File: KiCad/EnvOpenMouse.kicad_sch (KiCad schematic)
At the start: 55 parts, among them J11 Conn_02x02_Top_Bottom, J2 Button, J4 Conn_02x02_Top_Bottom, J5 Conn_02x02_Top_Bottom, J5 SKRKAEE020, J6 Conn_02x02_Top_Bottom, J7 Conn_02x02_Top_Bottom, J8 Conn_02x02_Top_Bottom, J9 Conn_01x03, SW1 SW_Push_SPDT, SW2 SW_Push_SPDT, SW3 SW_Push_SPDT, U1 AP2112K-3.3, U2 TLV70218DBVR, U3 RP2040, U4 PMW3360DM-T2QU, Y1 3225_4P 12MHz

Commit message: redid all traces, adjusted schematic, pinouts, added some side buttons.
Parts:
- removed C10, C11, C12, C13, C14, C5, C6, C7, C8, C9: 100nf 0402, Capacitor_SMD:C_0402_1005Metric, symbol Device:C
- removed C15, C16, C3: 1uf 0402, Capacitor_SMD:C_0402_1005Metric, symbol Device:C
- removed C19, C2: 22pf 0402, Capacitor_SMD:C_0402_1005Metric, symbol Device:C
- removed C2: 0.1uf 0402, Capacitor_SMD:C_0402_1005Metric, symbol Device:C
- removed C3: 10uf 0402 6.3V, Capacitor_SMD:C_0402_1005Metric, symbol Device:C
- removed C5: 10uf 0402, Capacitor_SMD:C_0402_1005Metric, symbol Device:C
- removed D1: 1n4002W, Diode_SMD:D_SOD-123, symbol Device:D_Schottky
- removed FLASH1: W25Q16JVUXIQ, Package_SON:SON-8-1EP_3x2mm_P0.5mm_EP1.4x1.6mm, symbol Memory_Flash:W25Q32JVZP
- removed J2: Button, Button_Switch_SMD:SW_Push_SPST_NO_Alps_SKRK, symbol Switch:SW_Push
- removed J5: SKRKAEE020, Button_Switch_SMD:SW_Push_SPST_NO_Alps_SKRK, symbol Switch:SW_Push
- removed R1, R3: 5.1K, Resistor_SMD:R_0402_1005Metric, symbol Device:R_Small
- removed R1, R11: 1K 0402, Resistor_SMD:R_0402_1005Metric, symbol Device:R
- removed R10, R9: 27Ohms 0402 Resistor, Capacitor_SMD:C_0402_1005Metric, symbol Device:R
- removed R2: 10K 0402, Resistor_SMD:R_0402_1005Metric, symbol Device:R
- removed R4: 10k 0402, Resistor_SMD:R_0402_1005Metric, symbol Device:R
- removed U1: AP2112K-3.3, Package_TO_SOT_SMD:SOT-23-5, symbol Regulator_Linear:AP2112K-3.3
- removed U2: TLV70218DBVR, Package_TO_SOT_SMD:SOT-23-5, symbol Regulator_Linear:TLV70218_SOT23-5
- removed U3: RP2040, RP2040_minimal:RP2040-QFN-56, symbol MCU_RaspberryPi_RP2040:RP2040
- removed Y1: 3225_4P 12MHz, Crystal:Crystal_SMD_3225-4Pin_3.2x2.5mm, symbol Device:Crystal_GND24
- removed e1: TYPE-C-31-M-12, HRO-TYPE-C31-M-12:HRO-TYPE-C-31-M-12, symbol Type-C:HRO-TYPE-C-31-M-12
- added H5, H6, H7, H8: MountingHole_Pad, MountingHole:MountingHole_2.2mm_M2, symbol Mechanical:MountingHole_Pad
- added J10, J12, J13: 0.8mm BM03B, Connector_JST:JST_SUR_BM03B-SURS-TF_1x03-1MP_P0.80mm_Vertical, symbol Connector_Generic:Conn_01x03
- added SW4, SW5, SW6, SW7: SW_Push_SPDT, Button_Switch_SMD:SW_SPST_B3U-1000P, symbol Switch:SW_Push
- J9: value Conn_01x03 -> 0.8mm BM03B; footprint Connector_PinHeader_1.27mm:PinHeader_1x03_P1.27mm_Vertical -> Connector_JST:JST_SUR_BM03B-SURS-TF_1x03-1MP_P0.80mm_Vertical
- SW1, SW2, SW3: symbol Switch:SW_Push_SPDT -> Switch:SW_Push
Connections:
- net MB-1-B_MB is gone; now on net GND: J8.1 (Pin_1)
- net MB-2-B_MB is gone; now on net GND: J7.4 (Pin_4)
- net MB-3-B_MB is gone; now on net GND: J8.4 (Pin_4)
- net GND: now also J5.4 (Pin_4), J6.1 (Pin_1), J6.4 (Pin_4), SW1.1, SW2.1, SW3.1, H5.1, H6.1, H7.1, H8.1, J10.2 (Pin_2), J12.2 (Pin_2), J13.2 (Pin_2), SW4.1, SW5.1, SW6.1, SW7.1
- net MB-1-A: now also SW1.2; no longer SW1.1 (A)
- net MB-2-A: now also SW2.2; no longer SW2.1 (A)
- net MB-3-A: now also SW3.2; no longer SW3.1 (A)
- removed net MB-1-B: J6.1 (Pin_1), SW1.2 (B)
- removed net MB-2-B: J5.4 (Pin_4), SW2.2 (B)
- removed net MB-3-B: J6.4 (Pin_4), SW3.2 (B)
- net SWCLK renamed SB-2-A
- net SB-2-A: now also SW5.2
- net SWD renamed SB-1-A
- net SB-1-A: now also SW4.2
- new net SB-1-A_MB: J12.1 (Pin_1)
- new net SB-2-A_MB: J12.3 (Pin_3)
- new net SB-3-A: J10.1 (Pin_1), SW6.2
- new net SB-3-A_MB: J13.1 (Pin_1)
- new net SB-4-A: J10.3 (Pin_3), SW7.2
- new net SB-4-A_MB: J13.3 (Pin_3)
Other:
- added sheet Power and USB (Power_USB.kicad_sch)
- added sheet RP2040 (RP2040.kicad_sch)
- note added: "IC to use - DRV2605L"
- note added: "LRM motor - C2682305"
- note added: "Main mouse buttons"
- note removed: "1.8V regulator"
- note removed: "1K resistor to prevent overdriving of the crystal as per the minimal design example"
- note removed: "2x 5.1K Resistors on the CC pins will = 5V@1.5A this is the recomended default config for type-c"
- note removed: "3.3V regulator"
- note removed: "Crystal"
- note removed: "D1 NEEDS to be 0omh resistor or 1n4002"
- note removed: "Flash"
- note removed: "KoreanHROParts USB_C_Receptacle_HRO_TYPE-C-31-M-12"
- note removed: "Make sure C10 is close to pin 44 of RP2040"
- note removed: "Make sure C3 is close to pin 45 of RP2040"
- note removed: "Make sure R3 and R4 are close to RP2040"
- note removed: "Make sure the flash chip you have selected supports 3.3V power or adjust the design."
- note removed: "Mouse Buttons"
- note removed: "Pin 9 technically doesnt exist its the main central contact under the chip for heat dicipation"
- note removed: "RP2040 supports 1MHz to 15MHz"
- note removed: "These decoupling capacitors are meant to be put close by each 3.3V pin of the RP2040"
- note removed: "USB/POWER"
- note removed: "not 22pf but pick to match crystal."
- note removed: "this is for factory testing always pull this to ground"
- moved on the sheet: C8, C9, H1, H2, H3, H4, J11, J4, J5, J6, J7, J8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

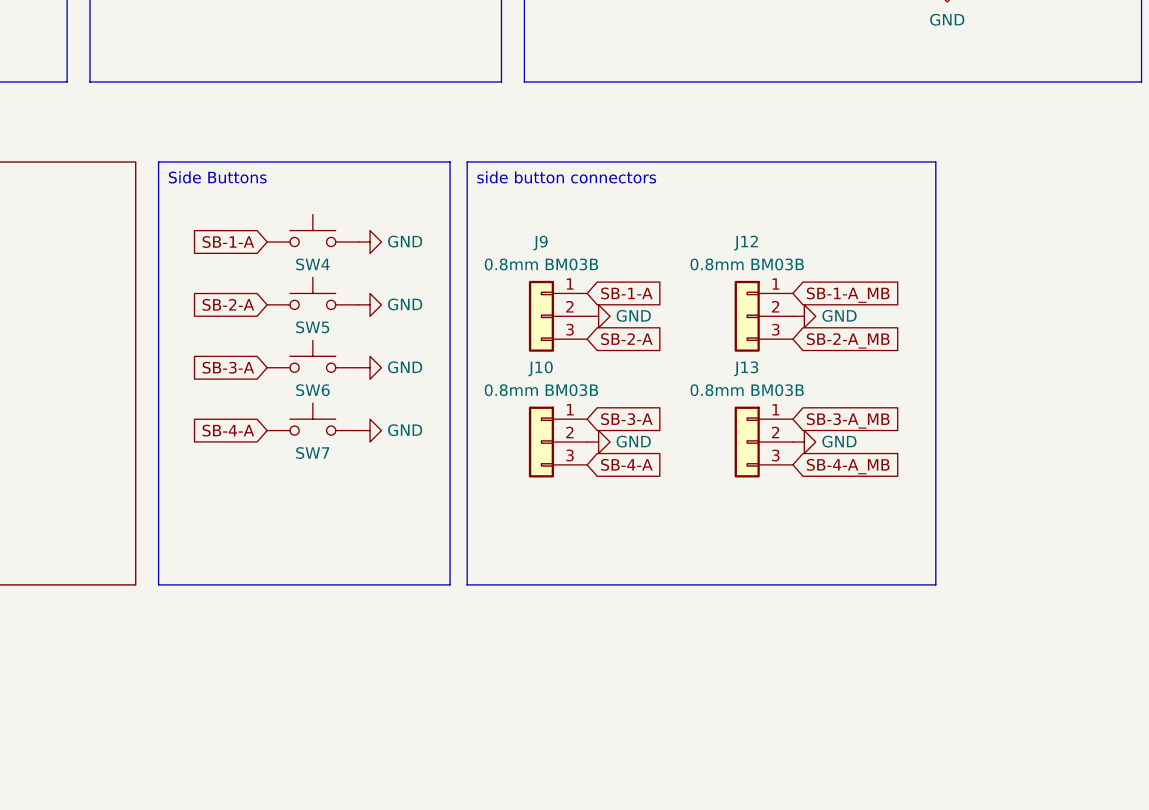
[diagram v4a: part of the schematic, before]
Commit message: downsized main board, added more buttons and respective connector, improved spacing of various power traces
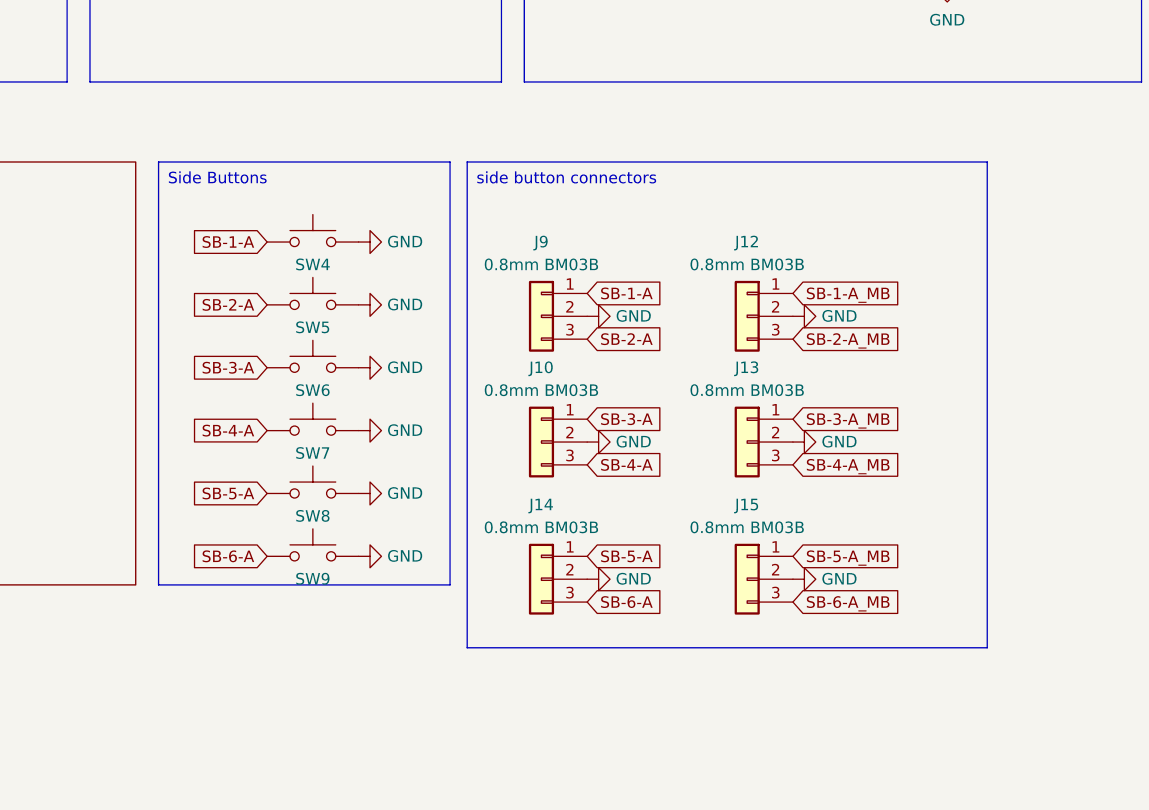
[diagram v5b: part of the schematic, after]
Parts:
- added J14, J15: 0.8mm BM03B, Connector_JST:JST_SUR_BM03B-SURS-TF_1x03-1MP_P0.80mm_Vertical, symbol Connector_Generic:Conn_01x03
- added SW8, SW9: SW_Push_SPDT, Button_Switch_SMD:SW_SPST_B3U-1000P, symbol Switch:SW_Push
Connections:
- net GND: now also J14.2 (Pin_2), J15.2 (Pin_2), SW8.1, SW9.1
- new net SB-5-A: J14.1 (Pin_1), SW8.2
- new net SB-5-A_MB: J15.1 (Pin_1)
- new net SB-6-A: J14.3 (Pin_3), SW9.2
- new net SB-6-A_MB: J15.3 (Pin_3)

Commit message: generated production files
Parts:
- J4: footprint Connector_PinHeader_1.27mm:PinHeader_1x02_P1.27mm_Vertical -> Connector_PinSocket_1.27mm:PinSocket_1x02_P1.27mm_Vertical
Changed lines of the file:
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@@
 			)
 		)
-		(property "Footprint" "Connector_PinHeader_1.27mm:PinHeader_1x02_P1.27mm_Vertical"
+		(property "Footprint" "Connector_PinSocket_1.27mm:PinSocket_1x02_P1.27mm_Vertical"
 			(at 36.83 30.48 0)
 			(effects

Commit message: final cleanups and other fixes
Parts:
- H1, H2, H3, H4, H5, H6, H7, H8: now left out of the parts list
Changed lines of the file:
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@@
 		(unit 1)
 		(exclude_from_sim no)
-		(in_bom yes)
+		(in_bom no)
 		(on_board yes)
 		(dnp no)
@@
 		(unit 1)
 		(exclude_from_sim no)
-		(in_bom yes)
+		(in_bom no)
 		(on_board yes)
 		(dnp no)
@@
 		(unit 1)
 		(exclude_from_sim no)
-		(in_bom yes)
+		(in_bom no)
 		(on_board yes)
 		(dnp no)
@@
 		(unit 1)
 		(exclude_from_sim no)
-		(in_bom yes)
+		(in_bom no)
 		(on_board yes)
 		(dnp no)
@@
 		(unit 1)
 		(exclude_from_sim no)
-		(in_bom yes)
+		(in_bom no)
 		(on_board yes)
 		(dnp no)
@@
 		(unit 1)
 		(exclude_from_sim no)
-		(in_bom yes)
+		(in_bom no)
 		(on_board yes)
 		(dnp no)
@@
 		(unit 1)
 		(exclude_from_sim no)
-		(in_bom yes)
+		(in_bom no)
 		(on_board yes)
 		(dnp no)
@@
 		(unit 1)
 		(exclude_from_sim no)
-		(in_bom yes)
+		(in_bom no)
 		(on_board yes)
 		(dnp no)

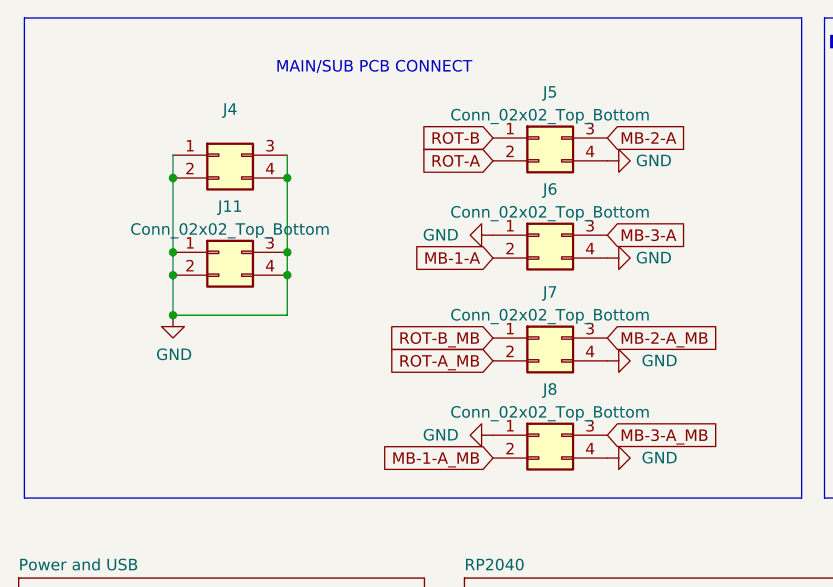
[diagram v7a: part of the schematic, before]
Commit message: updated part values, generated production files
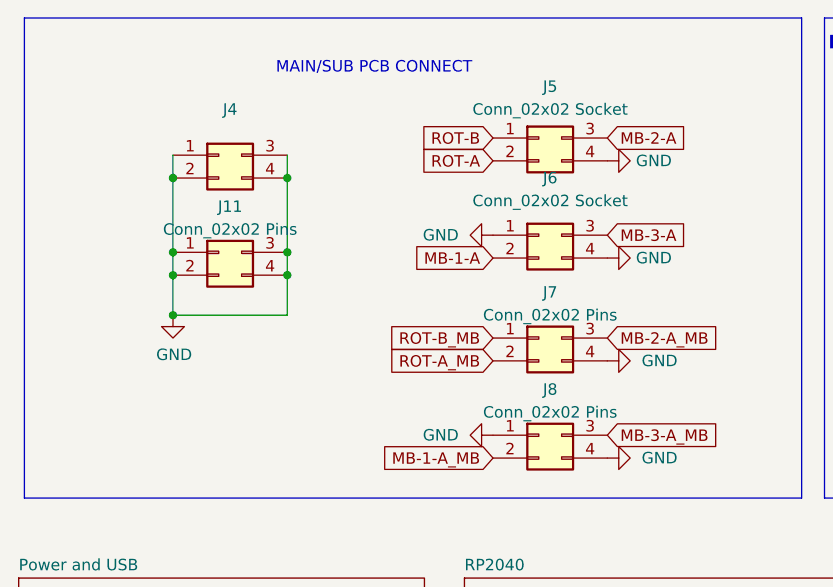
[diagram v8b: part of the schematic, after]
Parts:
- J11, J7, J8: value Conn_02x02_Top_Bottom -> Conn_02x02 Pins
- J4, J5, J6: value Conn_02x02_Top_Bottom -> Conn_02x02 Socket
- SW1, SW2, SW3: value SW_Push_SPDT -> Kailh GM switch
- SW4, SW5, SW6, SW7, SW8, SW9: value SW_Push_SPDT -> B3U-1000P
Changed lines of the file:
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@@
 			)
 		)
-		(property "Value" "SW_Push_SPDT"
+		(property "Value" "B3U-1000P"
 			(at 128.905 82.2476 0)
 			(effects
@@
 			)
 		)
-		(property "Value" "Conn_02x02_Top_Bottom"
+		(property "Value" "Conn_02x02 Socket"
 			(at 38.1 27.94 0)
 			(effects
@@
 			)
 		)
-		(property "Value" "SW_Push_SPDT"
+		(property "Value" "Kailh GM switch"
 			(at 115.57 22.225 0)
 			(effects
@@
 			)
 		)
-		(property "Value" "SW_Push_SPDT"
+		(property "Value" "B3U-1000P"
 			(at 128.905 89.2326 0)
 			(effects
@@
 			)
 		)
-		(property "Value" "SW_Push_SPDT"
+		(property "Value" "B3U-1000P"
 			(at 128.905 96.2176 0)
 			(effects
@@
 		(fields_autoplaced yes)
 		(property "Reference" "J5"
-			(at 73.66 23.495 0)
+			(at 73.66 22.86 0)
 			(effects
 				(font
@@
 			)
 		)
-		(property "Value" "Conn_02x02_Top_Bottom"
-			(at 73.66 26.035 0)
+		(property "Value" "Conn_02x02 Socket"
+			(at 73.66 25.4 0)
 			(effects
 				(font
@@
 			)
 		)
-		(property "Value" "SW_Push_SPDT"
+		(property "Value" "B3U-1000P"
 			(at 128.905 117.1726 0)
 			(effects
@@
 			)
 		)
-		(property "Value" "SW_Push_SPDT"
+		(property "Value" "B3U-1000P"
 			(at 128.905 103.2026 0)
 			(effects
@@
 			)
 		)
-		(property "Value" "Conn_02x02_Top_Bottom"
+		(property "Value" "Conn_02x02 Pins"
 			(at 73.66 48.26 0)
 			(effects
@@
 			)
 		)
-		(property "Value" "SW_Push_SPDT"
+		(property "Value" "Kailh GM switch"
 			(at 115.57 27.94 0)
 			(effects
@@
 			)
 		)
-		(property "Value" "SW_Push_SPDT"
+		(property "Value" "B3U-1000P"
 			(at 128.905 110.1876 0)
 			(effects
@@
 		(fields_autoplaced yes)
 		(property "Reference" "J6"
-			(at 73.66 34.29 0)
+			(at 73.66 33.02 0)
 			(effects
 				(font
@@
 			)
 		)
-		(property "Value" "Conn_02x02_Top_Bottom"
-			(at 73.66 36.83 0)
+		(property "Value" "Conn_02x02 Socket"
+			(at 73.66 35.56 0)
 			(effects
 				(font
@@
 			)
 		)
-		(property "Value" "SW_Push_SPDT"
+		(property "Value" "Kailh GM switch"
 			(at 115.57 34.925 0)
 			(effects
@@
 			)
 		)
-		(property "Value" "Conn_02x02_Top_Bottom"
+		(property "Value" "Conn_02x02 Pins"
 			(at 73.66 59.055 0)
 			(effects
@@
 			)
 		)
-		(property "Value" "Conn_02x02_Top_Bottom"
+		(property "Value" "Conn_02x02 Pins"
 			(at 38.1 38.735 0)
 			(effects
